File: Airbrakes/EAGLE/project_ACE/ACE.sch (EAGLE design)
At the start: 8 parts, among them J3 PTH

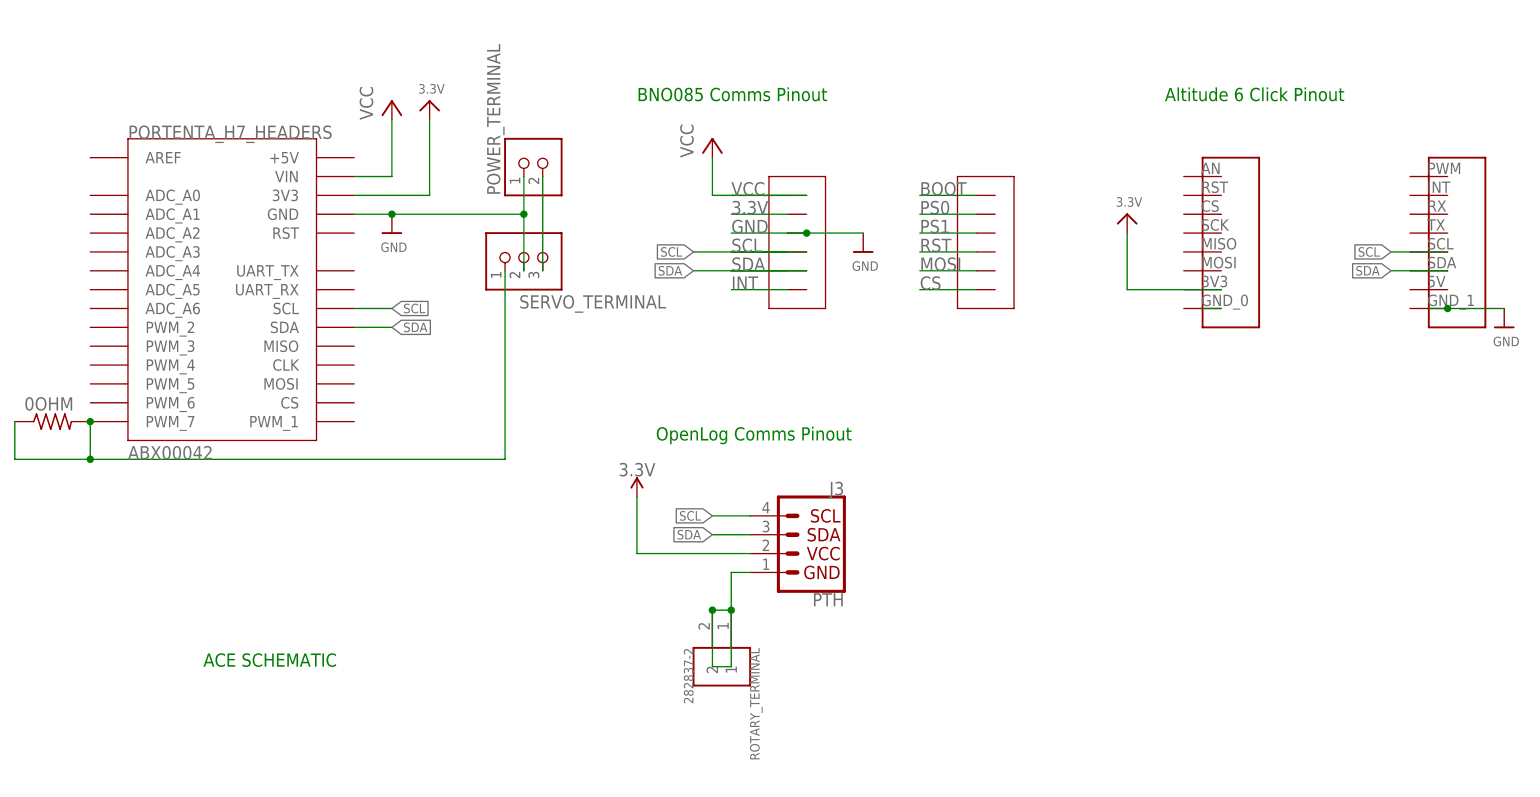
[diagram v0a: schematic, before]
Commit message: Finalized Review of v0.1.0 SS ACE
* Changed all terminal block to 200mil pitch
* Rerouted servo power switching
* Verify traces and add GND copper pour
* Spruce up silkscreen
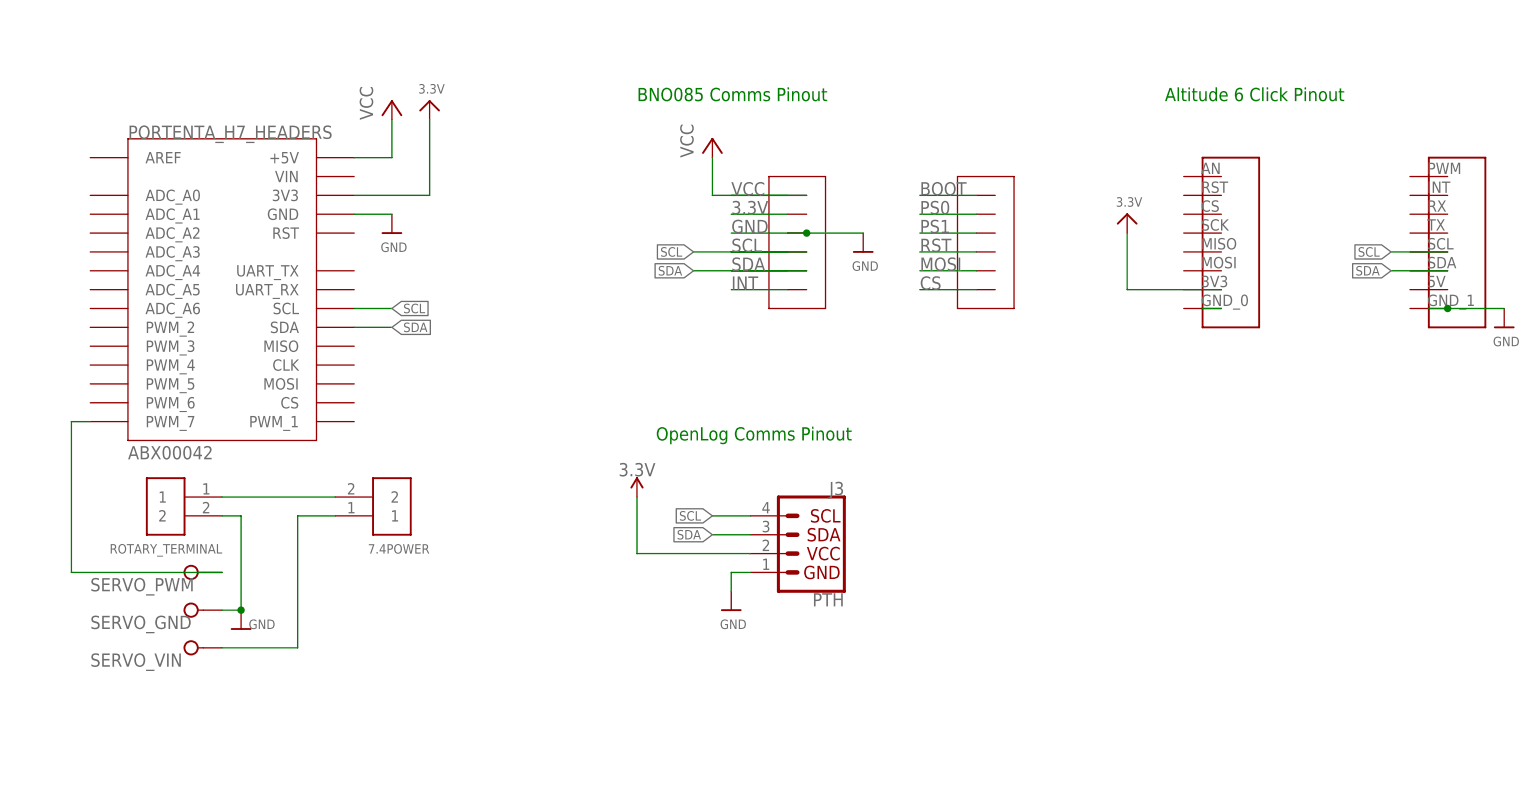
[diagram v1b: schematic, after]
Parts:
- removed 0OHM: (no value), fab_new:R1206
- removed POWER_TERMINAL: CONN_02_TERM-ADAFRUIT, fab_new:CONN_02_TERM-ADAFRUIT
- removed SERVO_TERMINAL: CONN_03_TERM'-FABLAB', fab_new:CONN_03_TERM'-FABLAB'
- added 7.4POWER: 282837-2, 282837-2:282837-2
- added SERVO: (no value), con-wago-508:W237-3E
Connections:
- removed net 7.4V: POWER_TERMINAL.2, SERVO_TERMINAL.3
- removed net N$2: J3.GND, ROTARY_TERMINAL.1, ROTARY_TERMINAL.2
- removed net PWM: 0OHM.1, 0OHM.2, SERVO_TERMINAL.1, U$10.PWM_7
- new net SERVO_GND: 7.4POWER.2, ROTARY_TERMINAL.1
- new net SERVO_PWM: SERVO-1.KL, U$10.PWM_7
- new net SERVO_VIN: 7.4POWER.1, SERVO-3.KL
- net GND: now also J3.GND, ROTARY_TERMINAL.2, SERVO-2.KL; no longer POWER_TERMINAL.1, SERVO_TERMINAL.2
- net VCC: now also U$10.+5V; no longer U$10.VIN
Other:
- note removed: "ACE SCHEMATIC"
- moved on the sheet: ROTARY_TERMINAL
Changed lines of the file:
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@@
 <part name="P+1" library="supply1" library_urn="urn:adsk.eagle:library:371" deviceset="VCC" device=""/>
 <part name="U$12" library="microbuilder" deviceset="GND" device=""/>
-<part name="POWER_TERMINAL" library="fab_new" deviceset="CONN_02_TERM" device="-ADAFRUIT"/>
-<part name="SERVO_TERMINAL" library="fab_new" deviceset="CONN_03_TERM" device="'-FABLAB'"/>
-<part name="0OHM" library="fab_new" deviceset="R" device="1206"/>
 <part name="U$1" library="MIKROE-4903" deviceset="MIKROE-ALTITUDE-6-CLICK-DVC" device=""/>
 <part name="ROTARY_TERMINAL" library="282837-2" deviceset="282837-2" device=""/>
+<part name="U$2" library="microbuilder" deviceset="GND" device=""/>
+<part name="U$6" library="microbuilder" deviceset="GND" device=""/>
+<part name="SERVO" library="con-wago-508" library_urn="urn:adsk.eagle:library:196" deviceset="W237-3E" device="" package3d_urn="urn:adsk.eagle:package:10747/1"/>
+<part name="7.4POWER" library="282837-2" deviceset="282837-2" device=""/>
 </parts>
 <sheets>
 <sheet>
 <plain>
-<text x="0" y="5.08" size="1.778" layer="91">ACE SCHEMATIC</text>
 <text x="60.96" y="35.56" size="1.778" layer="91">OpenLog Comms Pinout</text>
 <text x="58.42" y="81.28" size="1.778" layer="91">BNO085 Comms Pinout</text>
@@
 <attribute name="VALUE" x="23.876" y="60.96" size="1.27" layer="96"/>
 </instance>
-<instance part="POWER_TERMINAL" gate="G$1" x="45.72" y="71.12" smashed="yes" rot="R90">
-<attribute name="NAME" x="40.005" y="68.58" size="1.778" layer="95" rot="R90"/>
-</instance>
-<instance part="SERVO_TERMINAL" gate="G$1" x="43.18" y="58.42" smashed="yes" rot="R90">
-<attribute name="NAME" x="42.545" y="53.34" size="1.778" layer="95"/>
-</instance>
-<instance part="0OHM" gate="G$1" x="-20.32" y="38.1" smashed="yes">
-<attribute name="NAME" x="-24.13" y="39.5986" size="1.778" layer="95"/>
-<attribute name="VALUE" x="-24.13" y="34.798" size="1.778" layer="96"/>
-</instance>
 <instance part="U$1" gate="G$1" x="134.62" y="50.8" smashed="yes"/>
-<instance part="ROTARY_TERMINAL" gate="G$1" x="71.12" y="5.08" smashed="yes" rot="R270">
-<attribute name="NAME" x="73.66381875" y="7.620559375" size="1.271909375" layer="95" rot="R270"/>
-<attribute name="VALUE" x="64.745490625" y="7.62236875" size="1.274909375" layer="96" rot="R270"/>
+<instance part="ROTARY_TERMINAL" gate="G$1" x="-5.08" y="27.94" smashed="yes" rot="MR0">
+<attribute name="NAME" x="2.540559375" y="20.32381875" size="1.271909375" layer="95" rot="MR0"/>
+</instance>
+<instance part="U$2" gate="G$1" x="71.12" y="12.7" smashed="yes">
+<attribute name="VALUE" x="69.596" y="10.16" size="1.27" layer="96"/>
+</instance>
+<instance part="U$6" gate="G$1" x="5.08" y="10.16" smashed="yes">
+<attribute name="VALUE" x="6.096" y="10.16" size="1.27" layer="96"/>
+</instance>
+<instance part="SERVO" gate="-1" x="-2.54" y="17.78" smashed="yes"/>
+<instance part="SERVO" gate="-2" x="-2.54" y="12.7" smashed="yes"/>
+<instance part="SERVO" gate="-3" x="-2.54" y="7.62" smashed="yes">
+<attribute name="VALUE" x="-2.54" y="10.16" size="1.778" layer="96"/>
+</instance>
+<instance part="7.4POWER" gate="G$1" x="25.4" y="25.4" smashed="yes" rot="MR180">
+<attribute name="NAME" x="30.479440625" y="20.31618125" size="1.271909375" layer="95" rot="MR0"/>
 </instance>
 </instances>
@@
 <wire x1="20.32" y1="66.04" x2="25.4" y2="66.04" width="0.1524" layer="91"/>
 <pinref part="U$10" gate="G$1" pin="GND"/>
-<pinref part="POWER_TERMINAL" gate="G$1" pin="1"/>
-<pinref part="SERVO_TERMINAL" gate="G$1" pin="2"/>
-<wire x1="43.18" y1="58.42" x2="43.18" y2="66.04" width="0.1524" layer="91"/>
-<wire x1="43.18" y1="66.04" x2="43.18" y2="71.12" width="0.1524" layer="91"/>
-<wire x1="43.18" y1="66.04" x2="25.4" y2="66.04" width="0.1524" layer="91"/>
-<junction x="43.18" y="66.04"/>
-<junction x="25.4" y="66.04"/>
 </segment>
 <segment>
@@
 <junction x="167.64" y="53.34"/>
 </segment>
+<segment>
+<pinref part="J3" gate="G$1" pin="GND"/>
+<wire x1="73.66" y1="17.78" x2="71.12" y2="17.78" width="0.1524" layer="91"/>
+<pinref part="U$2" gate="G$1" pin="GND"/>
+<wire x1="71.12" y1="17.78" x2="71.12" y2="15.24" width="0.1524" layer="91"/>
+</segment>
+<segment>
+<pinref part="SERVO" gate="-2" pin="KL"/>
+<pinref part="U$6" gate="G$1" pin="GND"/>
+<wire x1="5.08" y1="12.7" x2="2.54" y2="12.7" width="0.1524" layer="91"/>
+<pinref part="ROTARY_TERMINAL" gate="G$1" pin="2"/>
+<wire x1="2.54" y1="25.4" x2="5.08" y2="25.4" width="0.1524" layer="91"/>
+<wire x1="5.08" y1="25.4" x2="5.08" y2="12.7" width="0.1524" layer="91"/>
+<junction x="5.08" y="12.7"/>
+</segment>
 </net>
 <net name="VCC" class="2">
@@
 </segment>
 <segment>
-<wire x1="25.4" y1="71.12" x2="25.4" y2="78.74" width="0.1524" layer="91"/>
+<pinref part="U$10" gate="G$1" pin="+5V"/>
 <pinref part="P+1" gate="VCC" pin="VCC"/>
-<pinref part="U$10" gate="G$1" pin="VIN"/>
-<wire x1="25.4" y1="71.12" x2="20.32" y2="71.12" width="0.1524" layer="91"/>
+<wire x1="20.32" y1="73.66" x2="25.4" y2="73.66" width="0.1524" layer="91"/>
+<wire x1="25.4" y1="73.66" x2="25.4" y2="78.74" width="0.1524" layer="91"/>
 </segment>
 </net>
@@
 </segment>
 </net>
-<net name="7.4V" class="0">
-<segment>
-<pinref part="POWER_TERMINAL" gate="G$1" pin="2"/>
-<pinref part="SERVO_TERMINAL" gate="G$1" pin="3"/>
-<wire x1="45.72" y1="71.12" x2="45.72" y2="58.42" width="0.1524" layer="91"/>
-</segment>
-</net>
-<net name="PWM" class="0">
-<segment>
-<pinref part="0OHM" gate="G$1" pin="1"/>
-<wire x1="-25.4" y1="38.1" x2="-25.4" y2="33.02" width="0.1524" layer="91"/>
-<wire x1="-25.4" y1="33.02" x2="-15.24" y2="33.02" width="0.1524" layer="91"/>
-<pinref part="SERVO_TERMINAL" gate="G$1" pin="1"/>
-<wire x1="-15.24" y1="33.02" x2="40.64" y2="33.02" width="0.1524" layer="91"/>
-<wire x1="40.64" y1="33.02" x2="40.64" y2="58.42" width="0.1524" layer="91"/>
-<pinref part="U$10" gate="G$1" pin="PWM_7"/>
-<pinref part="0OHM" gate="G$1" pin="2"/>
-<wire x1="-15.24" y1="38.1" x2="-15.24" y2="33.02" width="0.1524" layer="91"/>
-<junction x="-15.24" y="38.1"/>
-<junction x="-15.24" y="33.02"/>
-</segment>
-</net>
 <net name="N$4" class="2">
 <segment>
@@
 </segment>
 </net>
-<net name="N$2" class="2">
-<segment>
-<pinref part="J3" gate="G$1" pin="GND"/>
-<wire x1="73.66" y1="17.78" x2="71.12" y2="17.78" width="0.1524" layer="91"/>
+<net name="SERVO_PWM" class="0">
+<segment>
+<pinref part="U$10" gate="G$1" pin="PWM_7"/>
+<wire x1="-15.24" y1="38.1" x2="-17.78" y2="38.1" width="0.1524" layer="91"/>
+<wire x1="-17.78" y1="38.1" x2="-17.78" y2="17.78" width="0.1524" layer="91"/>
+<pinref part="SERVO" gate="-1" pin="KL"/>
+<wire x1="2.54" y1="17.78" x2="-17.78" y2="17.78" width="0.1524" layer="91"/>
+<label x="-15.24" y="15.24" size="1.778" layer="95"/>
+</segment>
+</net>
+<net name="SERVO_VIN" class="0">
+<segment>
+<wire x1="12.7" y1="25.4" x2="12.7" y2="7.62" width="0.1524" layer="91"/>
+<pinref part="SERVO" gate="-3" pin="KL"/>
+<wire x1="12.7" y1="7.62" x2="2.54" y2="7.62" width="0.1524" layer="91"/>
+<pinref part="7.4POWER" gate="G$1" pin="1"/>
+<wire x1="12.7" y1="25.4" x2="17.78" y2="25.4" width="0.1524" layer="91"/>
+<label x="-15.24" y="5.08" size="1.778" layer="95"/>
+</segment>
+</net>
+<net name="SERVO_GND" class="0">
+<segment>
+<pinref part="7.4POWER" gate="G$1" pin="2"/>
 <pinref part="ROTARY_TERMINAL" gate="G$1" pin="1"/>
-<wire x1="71.12" y1="17.78" x2="71.12" y2="12.7" width="0.1524" layer="91"/>
-<pinref part="ROTARY_TERMINAL" gate="G$1" pin="2"/>
-<wire x1="71.12" y1="12.7" x2="68.58" y2="12.7" width="0.1524" layer="91"/>
-<junction x="71.12" y="12.7"/>
-<wire x1="71.12" y1="12.7" x2="71.12" y2="5.08" width="0.1524" layer="91"/>
-<wire x1="71.12" y1="5.08" x2="68.58" y2="5.08" width="0.1524" layer="91"/>
-<wire x1="68.58" y1="5.08" x2="68.58" y2="12.7" width="0.1524" layer="91"/>
-<junction x="68.58" y="12.7"/>
+<wire x1="17.78" y1="27.94" x2="2.54" y2="27.94" width="0.1524" layer="91"/>
+<label x="-15.24" y="10.16" size="1.778" layer="95"/>
 </segment>
 </net>
@@
 will not be understood (or retained) with this version.
 </note>
+<note version="8.3" severity="warning">
+Since Version 8.3, EAGLE supports the association of 3D packages
+with devices in libraries, schematics, and board files. Those 3D
+packages will not be understood (or retained) with this version.
+</note>
 </compatibility>
